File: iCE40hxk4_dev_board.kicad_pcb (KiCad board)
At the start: 4 copper layers, 141 parts, among them J201 CONN_01X02, J202 USB_OTG, J401 CONN_01X35, J501 CONN_01X35, U201 MIC2005A-2, U203 93LCxxB_sot-23-6, U204 MIC5355/6-xYMME, U205 FT2232H, U301 iCE40-HX4K-TQ144, U302 25LC_EEPROM, U501 AS4C1M16S

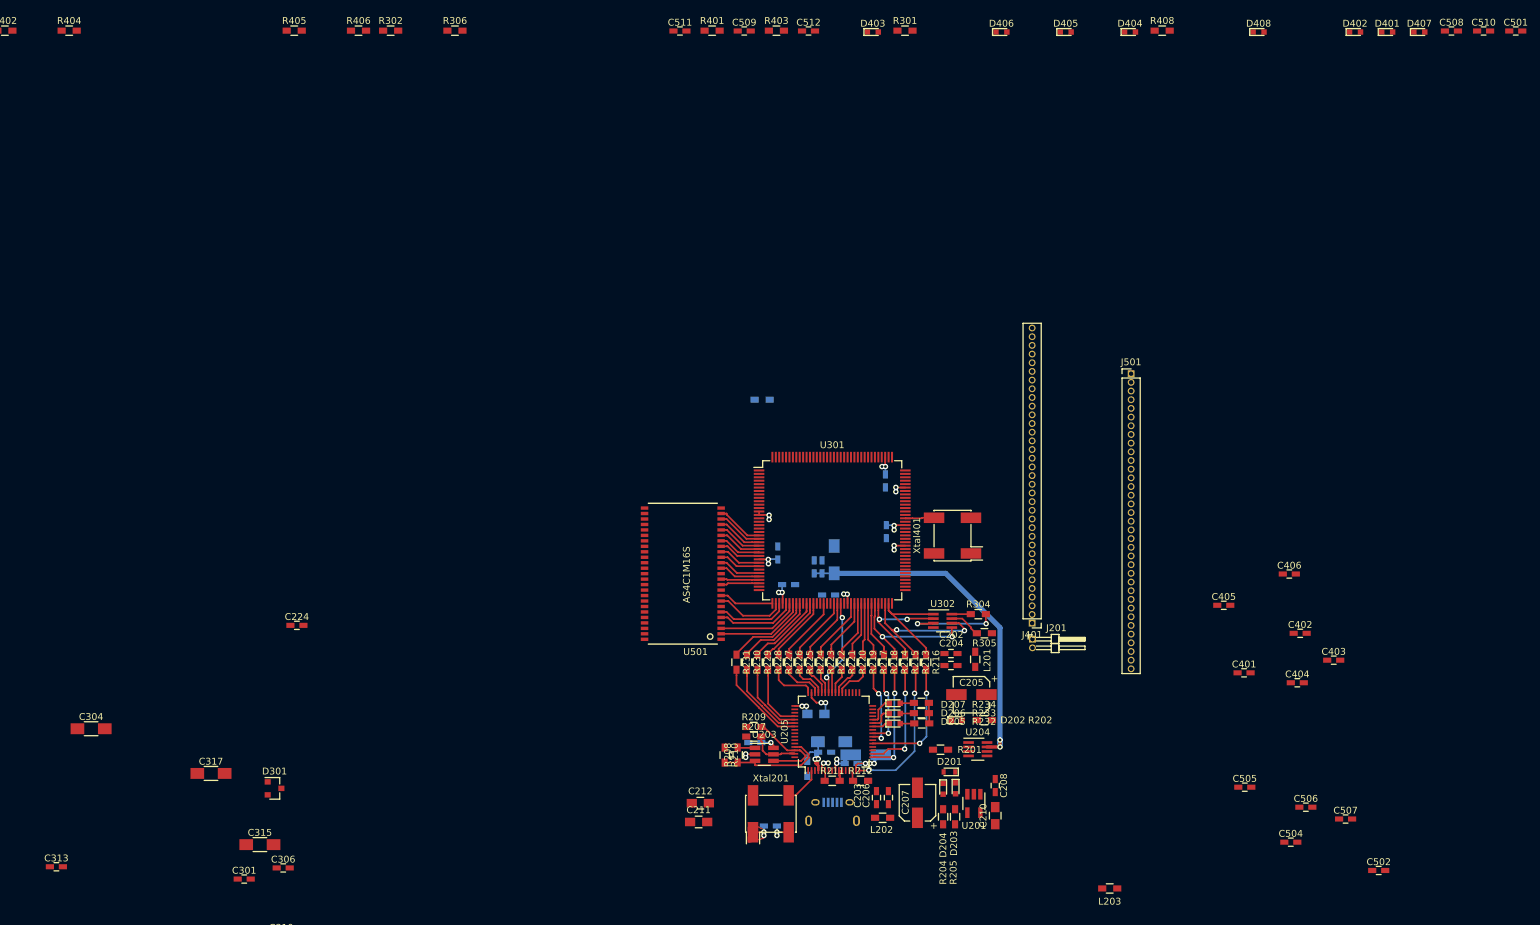
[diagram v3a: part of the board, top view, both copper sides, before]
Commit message: Changed MC2005 led fault, because it's an active low output and it's not active high. Placing of some capacitors and resistors. Check if it's possible to power the fpga in two layers (both 3.3 and 1.2 voltages).
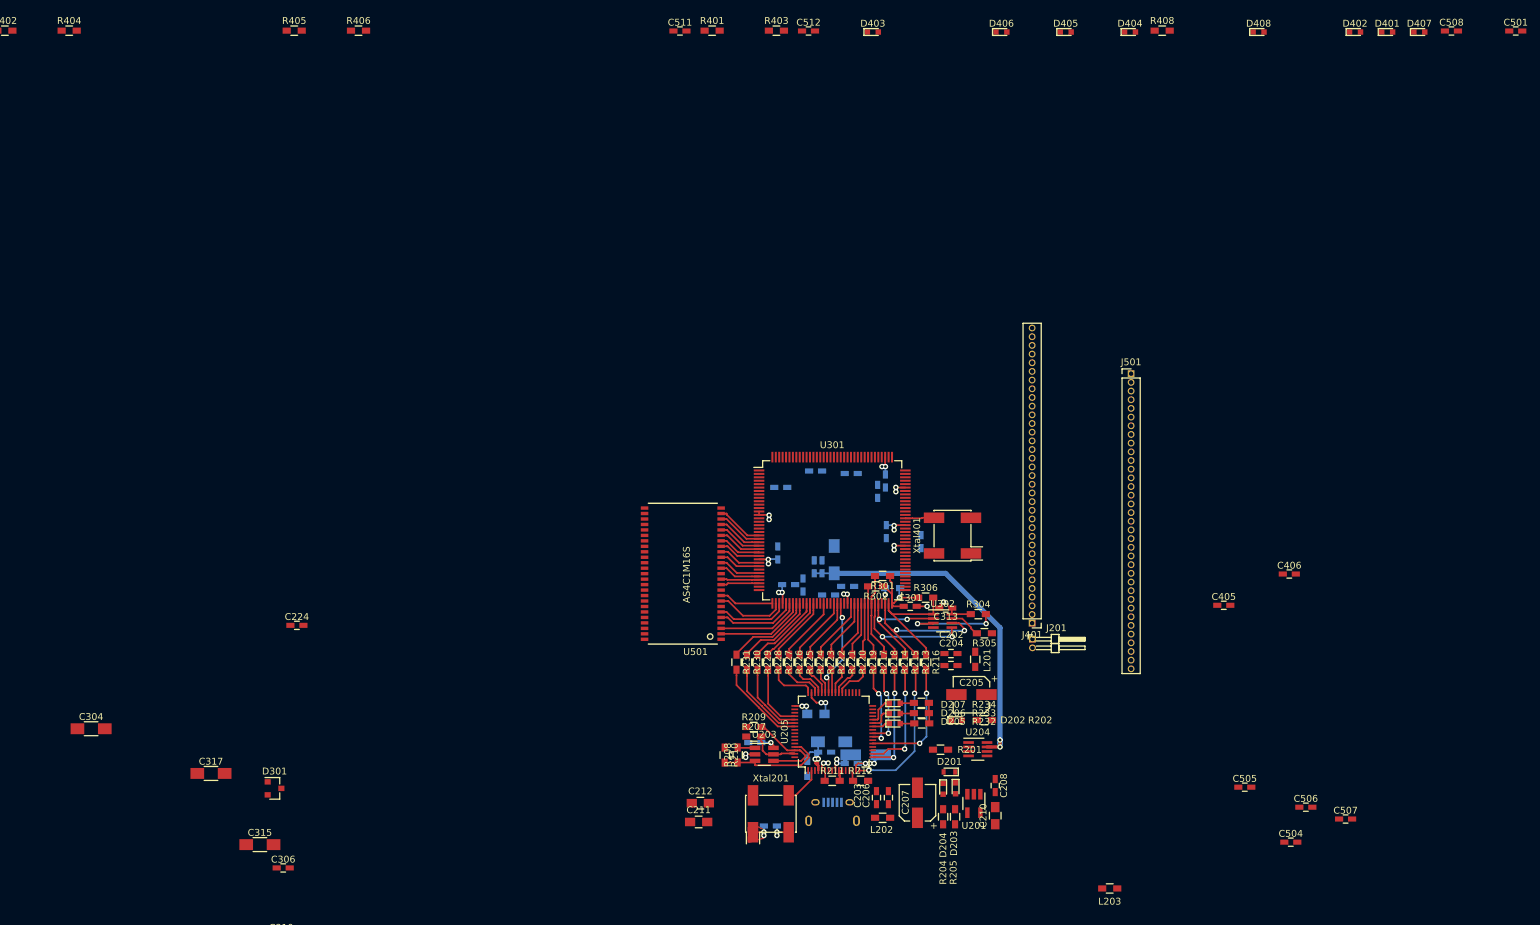
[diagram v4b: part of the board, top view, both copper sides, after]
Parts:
- C401, C402, C403, C404, C502, C509, C510: moved to B.Cu
- moved C313 135.5 mm to (193.9, 106.7), turned to 180 degrees
- moved C510 123.5 mm to (179.5, 103.5)
- moved R302 107.9 mm to (183.6, 103.5), turned to 180 degrees
- moved R306 107.8 mm to (190.9, 105.2)
- moved C301 105.3 mm to (188.7, 106.4)
- moved C502 103.9 mm to (169.7, 89.0)
- moved C509 81.5 mm to (173.0, 103.3), turned to 90 degrees
- moved R301 79.8 mm to (184.6, 102.0), turned to 180 degrees
- moved C403 71.1 mm to (183.9, 89.6), turned to 90 degrees
- moved C402 69.7 mm to (180.0, 87.0)
- moved C401 69.3 mm to (174.8, 86.6), turned to 180 degrees
- moved C404 58.8 mm to (190.2, 97.0), turned to 270 degrees
- moved R303 33.5 mm to (186.1, 103.8), turned to 180 degrees
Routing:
- net +3V3: track 25.5 -> 40.3 mm, vias 5 -> 6
- net /FPGA_PROGRAMMING+POWER/CRESET: track 8.28 -> 12.5 mm
- net GND: track 30.6 -> 33.3 mm, vias 19 -> 21
- net /FPGA_PROGRAMMING+POWER/CDONE: track 7.83 -> 10.3 mm
- net /FPGA_PROGRAMMING+POWER/SS: track 16.6 -> 19.0 mm
- net /FPGA_PROGRAMMING+POWER/SCK: track 22.5 -> 24.8 mm, vias 2 -> 3

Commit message: Continued with routing....
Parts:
- C203, C218, L202: moved to B.Cu
- moved C304 117.7 mm to (177.6, 79.4)
- moved C308 114.8 mm to (181.4, 81.3)
- moved C310 114.7 mm to (182.9, 79.1)
- moved C218 106.3 mm to (179.2, 122.7), turned to 270 degrees
- moved C306 102.1 mm to (177.2, 81.7)
- moved C219 55.6 mm to (179.2, 132.7), turned to 270 degrees
- moved C211 45.5 mm to (202.2, 128.3), turned to 270 degrees
- moved C212 42.0 mm to (198.6, 124.7), turned to 180 degrees
- moved C221 41.3 mm to (185.4, 142.0)
- moved C220 40.0 mm to (189.7, 143.3)
- moved C222 38.2 mm to (187.5, 145.0)
- moved C210 11.9 mm to (193.8, 127.6), turned to 270 degrees
- moved R201 9.99 mm to (198.4, 135.9)
- moved D201 9.12 mm to (198.1, 122.3), turned to 0 degrees
- moved C208 7.81 mm to (195.5, 127.3)
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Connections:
- D203 pad 1: GND -> Net-(D203-Pad1)
- D203 pad 2: Net-(D203-Pad2) -> /USB+OSCILLATOR+REGULATOR/+5V
- R205 pad 1: Net-(D203-Pad2) -> Net-(D203-Pad1)
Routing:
- net /USB+OSCILLATOR+REGULATOR/+5V: track 0.00 -> 35.6 mm
- net /USB+OSCILLATOR+REGULATOR/Vext_filtered: track 0.00 -> 31.0 mm
- net Net-(C202-Pad1): track 0.00 -> 8.60 mm
- net /USB+OSCILLATOR+REGULATOR/Vbus_filtered: track 0.00 -> 6.67 mm, vias 0 -> 1
- net /USB+OSCILLATOR+REGULATOR/D-: track 0.00 -> 4.83 mm, vias 0 -> 1
- net /USB+OSCILLATOR+REGULATOR/D+: track 0.00 -> 4.79 mm, vias 0 -> 1
- net +1.8V: track 2.91 -> 7.57 mm, vias 2 -> 4
- net GND: track 33.3 -> 29.6 mm
- net Net-(C203-Pad1): track 0.00 -> 3.70 mm
- net +3V3: track 40.3 -> 41.9 mm
- net Net-(D204-Pad2): track 0.00 -> 1.40 mm
- net Net-(D202-Pad2): track 0.00 -> 1.36 mm
- net Net-(R205-Pad2): track 0.00 -> 1.34 mm
- net Net-(D203-Pad1): track 0.00 -> 1.24 mm
- net /FPGA_PROGRAMMING+POWER/+1.2V: track 64.1 -> 64.0 mm, vias 10 -> 9

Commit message: Continued with routing...
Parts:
- C201: moved to F.Cu
- C220, C221, C222, C223, C224, C315, C501, C504, C505, L203, R301, R302, R307, R401, R402, R403, R404, R405, R406, R407, R408: moved to B.Cu
- moved C407 187.8 mm to (199.0, 91.9), turned to 90 degrees
- moved R402 160.5 mm to (194.6, 103.4)
- moved R307 160.2 mm to (175.5, 103.4)
- moved C503 151.3 mm to (148.3, 107.4), turned to 270 degrees
- moved R404 151.1 mm to (194.7, 100.8)
- moved R308 146.5 mm to (181.6, 79.5), turned to 180 degrees
- moved C508 144.1 mm to (148.3, 102.7), turned to 270 degrees
- moved C501 136.6 mm to (166.5, 102.2), turned to 270 degrees
- moved R405 123.5 mm to (194.7, 99.7)
- moved C316 120.7 mm to (177.4, 82.9), turned to 180 degrees
- moved R406 115.6 mm to (194.7, 98.6)
- moved D301 109.2 mm to (192.9, 83.5), turned to 180 degrees
- moved C317 104.7 mm to (178.6, 81.2), turned to 180 degrees
- moved D401 104.1 mm to (194.7, 104.6)
- moved C507 103.3 mm to (160.0, 91.2), turned to 180 degrees
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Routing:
- net +3V3: track 41.9 -> 79.5 mm, vias 6 -> 18
- net GND: track 29.6 -> 50.7 mm, vias 21 -> 24
- net Net-(C213-Pad1): track 14.2 -> 3.46 mm, vias 2 -> 1
- net Net-(C314-Pad1): track 0.00 -> 8.40 mm, vias 0 -> 1
- net Net-(C316-Pad1): track 0.00 -> 7.78 mm
- net /RIGHT_TOP_BANKs/IOR_117: track 0.00 -> 7.67 mm
- net /RIGHT_TOP_BANKs/IOR_116: track 0.00 -> 7.35 mm
- net /RIGHT_TOP_BANKs/IOR_115: track 0.00 -> 6.98 mm
- net /RIGHT_TOP_BANKs/IOR_114: track 0.00 -> 6.71 mm
- net /RIGHT_TOP_BANKs/IOR_112: track 0.00 -> 6.69 mm
- net /RIGHT_TOP_BANKs/IOR_111: track 0.00 -> 6.33 mm
- net /RIGHT_TOP_BANKs/IOR_109: track 0.00 -> 6.32 mm
- net /RIGHT_TOP_BANKs/IOR_110: track 0.00 -> 6.01 mm
- net Net-(D301-Pad1): track 0.00 -> 5.85 mm
- net Net-(C314-Pad2): track 0.00 -> 4.86 mm, vias 0 -> 1
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- removed copper zone on F.Cu, net +3V3

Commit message: Continued with routing...
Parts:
- C304, C306, C308, C310: moved to B.Cu
- moved C304 11.4 mm to (173.4, 91.9), turned to 270 degrees
- moved C306 11.2 mm to (171.7, 90.6), turned to 90 degrees
- moved C310 9.18 mm to (166.5, 88.0), turned to 90 degrees
- moved C308 8.38 mm to (170.4, 90.6), turned to 90 degrees
- moved C312 7.59 mm to (169.2, 105.9), turned to 180 degrees
- moved C502 1.53 mm to (165.1, 88.0)
- moved C311 1.27 mm to (169.2, 107.2)
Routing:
- net GND: track 50.7 -> 51.9 mm
- net /FPGA_PROGRAMMING+POWER/+1.2V: track 64.3 -> 65.6 mm

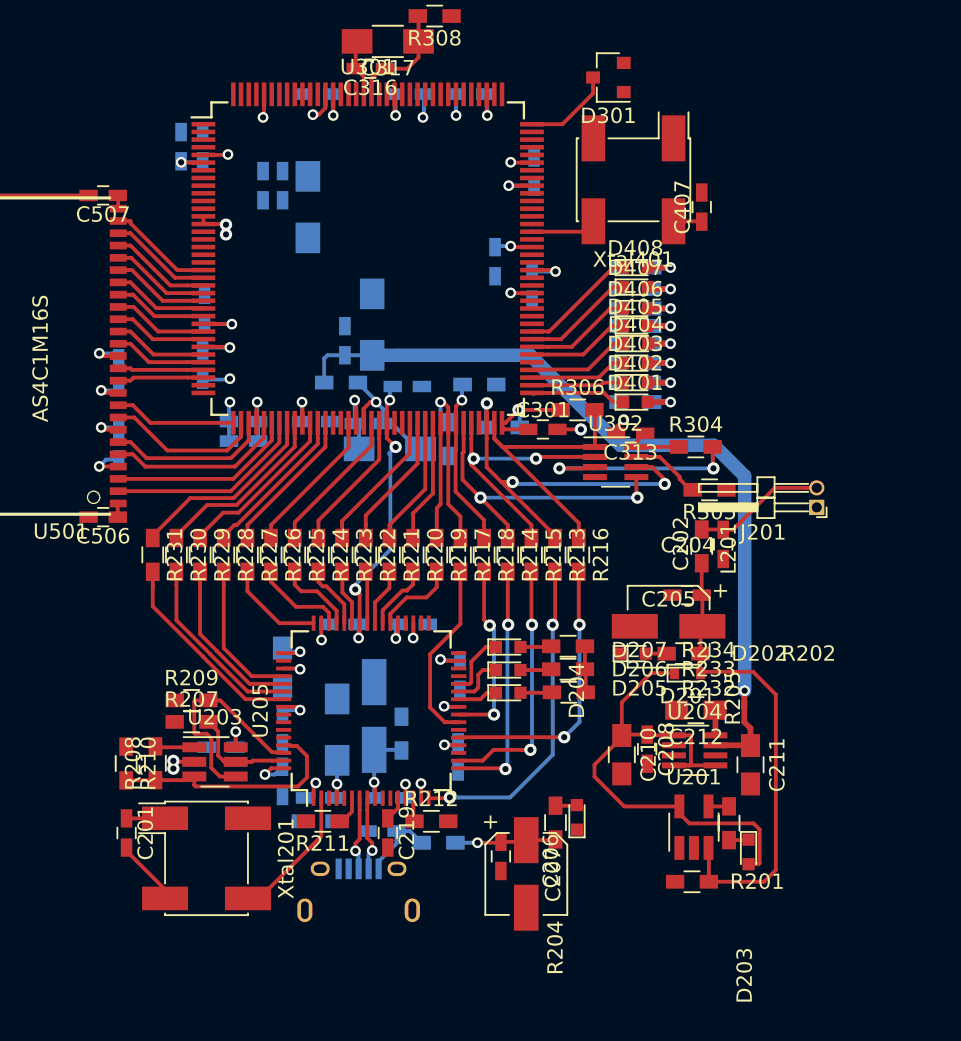
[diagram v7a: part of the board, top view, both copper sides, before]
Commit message: Replacement of many components. It's not finished
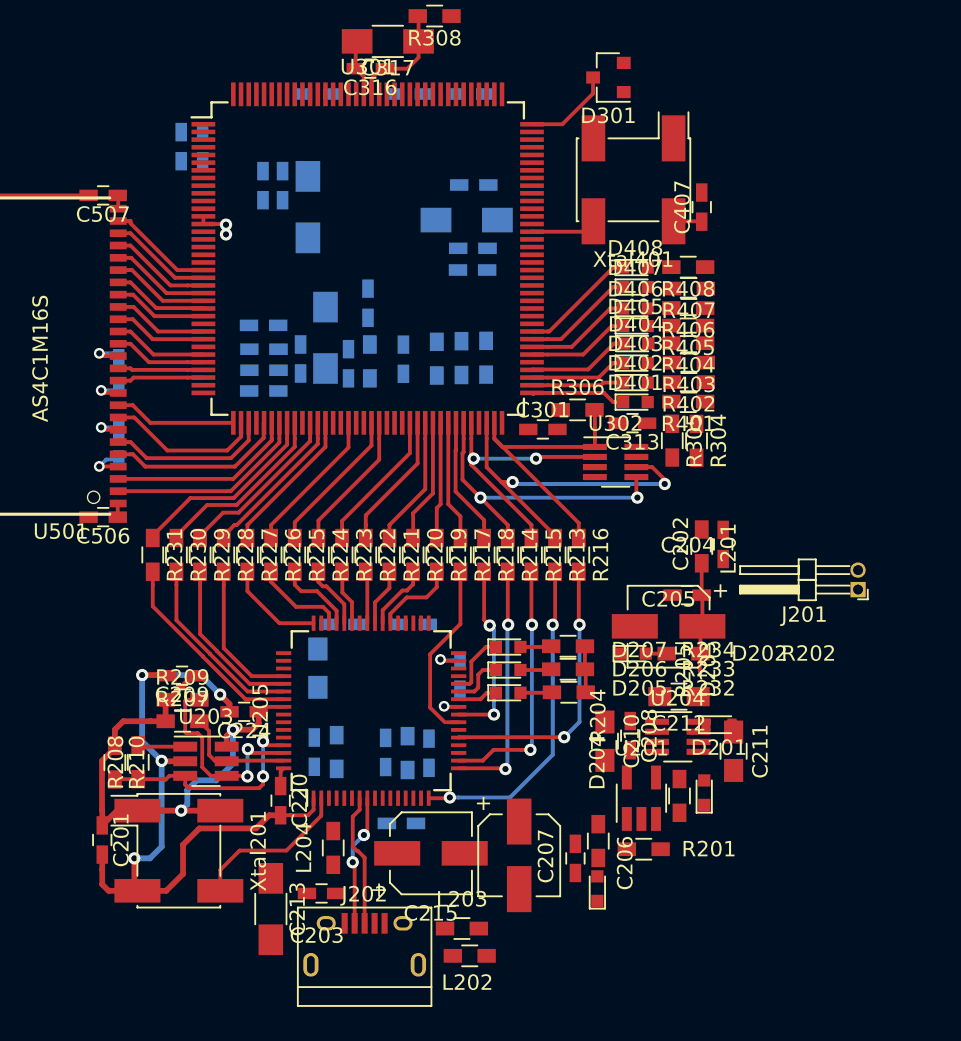
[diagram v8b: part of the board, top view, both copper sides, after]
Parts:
- C203, C209, C213, C215, C220, C224, J202, L202, L203, L204, R401, R402, R403, R404, R405, R406, R407, R408: moved to F.Cu
- C219, R211, R212: moved to B.Cu
- moved L203 13.3 mm to (183.4, 138.9), turned to 0 degrees
- moved C213 12.5 mm to (170.9, 137.7), turned to 270 degrees
- moved C215 9.68 mm to (181.4, 134.0), turned to 0 degrees
- moved C302 9.18 mm to (183.7, 92.8), turned to 180 degrees
- moved C315 8.36 mm to (174.5, 100.5), turned to 270 degrees
- moved L202 7.64 mm to (183.9, 140.7)
- moved J201 5.99 mm to (209.2, 116.9)
- moved C203 5.66 mm to (174.2, 136.7)
- moved C209 5.31 mm to (165.2, 122.5)
- moved R302 5.29 mm to (181.8, 101.8), turned to 270 degrees
- moved C219 5.25 mm to (178.4, 127.5), turned to 90 degrees
- moved C206 4.85 mm to (190.8, 134.4)
- moved D204 4.83 mm to (192.2, 136.3)
- moved D203 4.82 mm to (199.2, 130.1), turned to 90 degrees
- moved R212 4.71 mm to (179.8, 127.5), turned to 90 degrees
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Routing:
- net /FPGA_PROGRAMMING+POWER/+1.2V: track 65.6 -> 0.00 mm, vias 5 -> 0
- net /USB+OSCILLATOR+REGULATOR/+5V: track 35.6 -> 0.00 mm
- net +3V3: track 79.5 -> 52.6 mm, vias 18 -> 5
- net /USB+OSCILLATOR+REGULATOR/Vext_filtered: track 31.0 -> 7.09 mm
- net GND: track 51.9 -> 68.0 mm, vias 24 -> 9
- net Net-(R304-Pad2): track 13.8 -> 0.00 mm, vias 2 -> 0
- net Net-(C202-Pad1): track 8.60 -> 0.00 mm
- net Net-(C314-Pad1): track 8.40 -> 0.04 mm, vias 1 -> 0
- net +1.8V: track 8.73 -> 1.24 mm, vias 3 -> 0
- net /USB+OSCILLATOR+REGULATOR/Vbus_filtered: track 6.67 -> 0.00 mm, vias 1 -> 0
- net Net-(C215-Pad1): track 6.02 -> 0.00 mm, vias 1 -> 0
- net Net-(C203-Pad1): track 5.41 -> 0.00 mm
- net Net-(C314-Pad2): track 4.86 -> 0.00 mm, vias 1 -> 0
- net Net-(R305-Pad2): track 4.64 -> 0.00 mm
- net /USB+OSCILLATOR+REGULATOR/D+: track 4.79 -> 8.69 mm, vias 1 -> 0
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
